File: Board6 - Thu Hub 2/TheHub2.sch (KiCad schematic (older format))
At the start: 26 parts, among them J1 12V Power, J2 SERVO, J3 I2C, U1 BNO055-Breakout, U2 FeatherM0, U3 RFM95-Breakout, U4 AZ1117-3.3, U5 L7806, U6 GT-U7_GPS

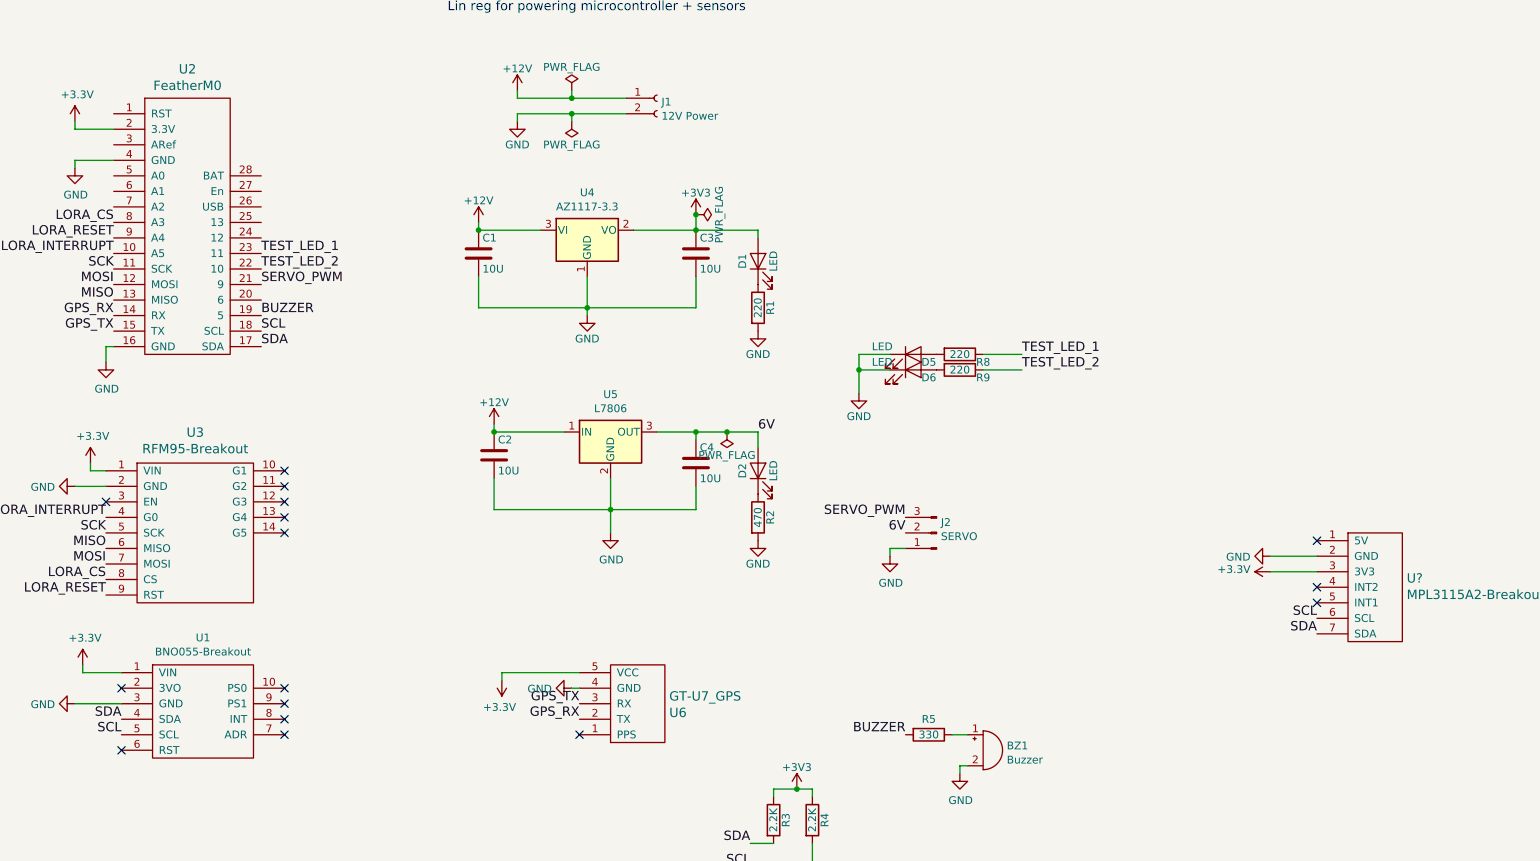
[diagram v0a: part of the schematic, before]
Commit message: For Hub2: add servo2 and GPS changed to breakout for MAX M8Q
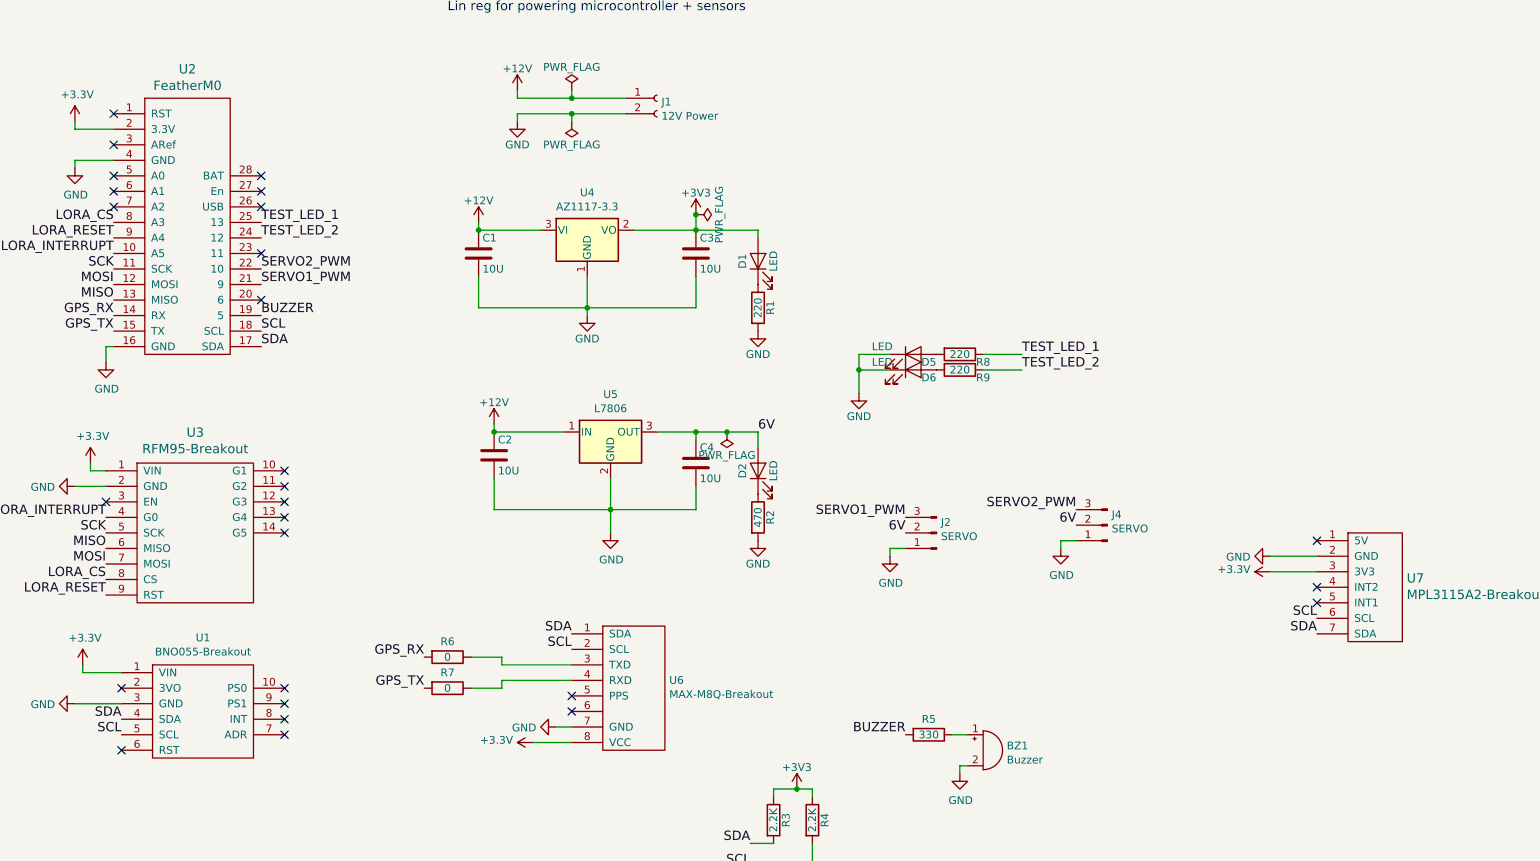
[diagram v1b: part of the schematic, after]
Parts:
- removed U6: GT-U7_GPS, DannysLib:GPS_GT-07, symbol Danny's_Lib:GT-U7_GPS
- added J4: SERVO, Pin_Headers:Pin_Header_Straight_1x03_Pitch2.54mm, symbol Connector:Conn_01x03_Male
- added R6, R7: 0, Resistors_SMD:R_0805, symbol Device:R
- added U6: MAX-M8Q-Breakout, DannysLib:MAX-M8Q-Breakout, symbol Danny's_Lib:MAX-M8Q-Breakout
- U7: renamed from U?; footprint (none) -> DannysLib:MPL3115A2-Breakout
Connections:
- net +3V3: now also U6.8 (VCC)
- net 6V: now also J4.2 (Pin_2)
- net GND: now also J4.1 (Pin_1), U6.7 (GND)
- net GPS_RX: now also R6.2
- net GPS_TX: now also R7.2
- net SCL: now also U6.2 (SCL)
- net SDA: now also U6.1 (SDA)
- net TEST_LED_1: now also U2.25 (13); no longer U2.23 (11)
- net TEST_LED_2: now also U2.24 (12); no longer U2.22 (10)
- net SERVO_PWM renamed SERVO1_PWM
- new net: R6.1, U6.3 (TXD)
- new net: R7.1, U6.4 (RXD)
- new net SERVO2_PWM: J4.3 (Pin_3), U2.22 (10)
- no-connect marks 16 -> 27
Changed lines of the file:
@@
 	9100 6650 8900 6650
 Text Label 10250 7200 2    60   ~ 0
-SERVO_PWM
+SERVO1_PWM
 Text Label 10250 7300 2    60   ~ 0
 6V
@@
 	10150 7400 10250 7400
 $Comp
-L Danny's_Lib:GT-U7_GPS U6
-U 1 1 5CB0ED28
-P 8550 8400
-F 0 "U6" H 8728 8458 60  0000 L CNN
-F 1 "GT-U7_GPS" H 8728 8352 60  0000 L CNN
-F 2 "DannysLib:GPS_GT-07" H 8700 8150 60  0001 C CNN
-F 3 "" H 8700 8150 60  0001 C CNN
-	1    8550 8400
-	1    0    0    1
-$EndComp
-NoConn ~ 8150 8600
-$Comp
 L Danny's_Lib:FeatherM0 U2
 U 1 1 5CB12923
@@
 Text Label 5150 6000 2    60   ~ 0
 GPS_TX
-Text Label 8150 8400 2    60   ~ 0
+Text Label 7150 8300 2    60   ~ 0
 GPS_TX
-Text Label 8150 8500 2    60   ~ 0
+Text Label 7150 8100 2    60   ~ 0
 GPS_RX
 Text Label 5150 5900 2    60   ~ 0
 GPS_RX
-$Comp
-L power:GND #PWR014
-U 1 1 5CB18900
-P 8100 8300
-F 0 "#PWR014" H 8100 8050 50  0001 C CNN
-F 1 "GND" V 8105 8172 50  0000 R CNN
-F 2 "" H 8100 8300 50  0001 C CNN
-F 3 "" H 8100 8300 50  0001 C CNN
-	1    8100 8300
-	0    1    1    0
-$EndComp
-Wire Wire Line
-	8100 8300 8150 8300
-$Comp
-L power:+3.3V #PWR013
-U 1 1 5CB1A329
-P 7650 8250
-F 0 "#PWR013" H 7650 8100 50  0001 C CNN
-F 1 "+3.3V" H 7665 8423 50  0000 C CNN
-F 2 "" H 7650 8250 50  0001 C CNN
-F 3 "" H 7650 8250 50  0001 C CNN
-	1    7650 8250
-	-1   0    0    1
-$EndComp
-Wire Wire Line
-	7650 8250 7650 8200
-Wire Wire Line
-	7650 8200 8150 8200
 $Comp
 L power:GND #PWR011
@@
 BUZZER
 Text Label 6100 5700 0    60   ~ 0
-SERVO_PWM
+SERVO1_PWM
 Text Label 11000 6150 0    60   ~ 0
 TEST_LED_1
-Text Label 6100 5600 0    60   ~ 0
+Text Label 6100 5400 0    60   ~ 0
 TEST_LED_2
-Text Label 6100 5500 0    60   ~ 0
+Text Label 6100 5300 0    60   ~ 0
 TEST_LED_1
 $Comp
@@
 	4900 4900 5150 4900
 $Comp
-L Danny's_Lib:MPL3115A2-Breakout U?
+L Danny's_Lib:MPL3115A2-Breakout U7
 U 1 1 5CC5A3F2
 P 13250 7650
-F 0 "U?" H 13478 7708 60  0000 L CNN
+F 0 "U7" H 13478 7708 60  0000 L CNN
 F 1 "MPL3115A2-Breakout" H 13478 7602 60  0000 L CNN
-F 2 "" V 13100 7500 60  0001 C CNN
+F 2 "DannysLib:MPL3115A2-Breakout" V 13100 7500 60  0001 C CNN
 F 3 "" V 13100 7500 60  0001 C CNN
 	1    13250 7650
@@
 $EndComp
 $Comp
-L power:+3.3V #PWR?
+L power:+3.3V #PWR0103
 U 1 1 5CC5AE7C
 P 12600 7550
-F 0 "#PWR?" H 12600 7400 50  0001 C CNN
+F 0 "#PWR0103" H 12600 7400 50  0001 C CNN
 F 1 "+3.3V" V 12615 7678 50  0000 L CNN
 F 2 "" H 12600 7550 50  0001 C CNN
@@
 	12600 7550 12900 7550
 $Comp
-L power:GND #PWR?
+L power:GND #PWR0104
 U 1 1 5CC5D6E7
 P 12600 7450
-F 0 "#PWR?" H 12600 7200 50  0001 C CNN
+F 0 "#PWR0104" H 12600 7200 50  0001 C CNN
 F 1 "GND" V 12605 7322 50  0000 R CNN
 F 2 "" H 12600 7450 50  0001 C CNN
@@
 NoConn ~ 12900 7650
 NoConn ~ 12900 7350
+Text Label 11350 7150 2    60   ~ 0
+SERVO2_PWM
+Text Label 11350 7250 2    60   ~ 0
+6V
+$Comp
+L power:GND #PWR0105
+U 1 1 5CAC3301
+P 11250 7400
+F 0 "#PWR0105" H 11250 7150 50  0001 C CNN
+F 1 "GND" H 11255 7227 50  0000 C CNN
+F 2 "" H 11250 7400 50  0001 C CNN
+F 3 "" H 11250 7400 50  0001 C CNN
+	1    11250 7400
+	1    0    0    -1
+$EndComp
+Wire Wire Line
+	11250 7400 11250 7350
+Wire Wire Line
+	11250 7350 11350 7350
+$Comp
+L Connector:Conn_01x03_Male J4
+U 1 1 5CAC3309
+P 11550 7250
+F 0 "J4" H 11522 7182 50  0000 R CNN
+F 1 "SERVO" H 11522 7273 50  0000 R CNN
+F 2 "Pin_Headers:Pin_Header_Straight_1x03_Pitch2.54mm" H 11550 7250 50  0001 C CNN
+F 3 "~" H 11550 7250 50  0001 C CNN
+	1    11550 7250
+	-1   0    0    1
+$EndComp
+Text Label 6100 5600 0    60   ~ 0
+SERVO2_PWM
+$Comp
+L Danny's_Lib:MAX-M8Q-Breakout U6
+U 1 1 5CAC4EC0
+P 8500 8300
+F 0 "U6" H 8728 8351 50  0000 L CNN
+F 1 "MAX-M8Q-Breakout" H 8728 8260 50  0000 L CNN
+F 2 "DannysLib:MAX-M8Q-Breakout" H 8550 8350 50  0001 C CNN
+F 3 "" H 8550 8350 50  0001 C CNN
+	1    8500 8300
+	1    0    0    -1
+$EndComp
+Text Label 8100 7950 2    60   ~ 0
+SDA
+Text Label 8100 8050 2    60   ~ 0
+SCL
+NoConn ~ 8100 8350
+NoConn ~ 8100 8450
+$Comp
+L power:GND #PWR0106
+U 1 1 5CAC9F48
+P 8000 8550
+F 0 "#PWR0106" H 8000 8300 50  0001 C CNN
+F 1 "GND" V 8005 8422 50  0000 R CNN
+F 2 "" H 8000 8550 50  0001 C CNN
+F 3 "" H 8000 8550 50  0001 C CNN
+	1    8000 8550
+	0    1    1    0
+$EndComp
+Wire Wire Line
+	8000 8550 8100 8550
+$Comp
+L power:+3.3V #PWR0107
+U 1 1 5CACBF38
+P 7850 8650
+F 0 "#PWR0107" H 7850 8500 50  0001 C CNN
+F 1 "+3.3V" V 7865 8778 50  0000 L CNN
+F 2 "" H 7850 8650 50  0001 C CNN
+F 3 "" H 7850 8650 50  0001 C CNN
+	1    7850 8650
+	0    -1   -1   0
+$EndComp
+Wire Wire Line
+	7850 8650 8100 8650
+$Comp
+L Device:R R6
+U 1 1 5CAD4F0B
+P 7300 8100
+F 0 "R6" V 7200 8100 50  0000 C CNN
+F 1 "0" V 7300 8100 50  0000 C CNN
+F 2 "Resistors_SMD:R_0805" V 7230 8100 50  0001 C CNN
+F 3 "~" H 7300 8100 50  0001 C CNN
+	1    7300 8100
+	0    1    1    0
+$EndComp
+$Comp
+L Device:R R7
+U 1 1 5CAD7B5D
+P 7300 8300
+F 0 "R7" V 7200 8300 50  0000 C CNN
+F 1 "0" V 7300 8300 50  0000 C CNN
+F 2 "Resistors_SMD:R_0805" V 7230 8300 50  0001 C CNN
+F 3 "~" H 7300 8300 50  0001 C CNN
+	1    7300 8300
+	0    1    1    0
+$EndComp
+Wire Wire Line
+	7450 8300 7650 8300
+Wire Wire Line
+	7650 8300 7650 8250
+Wire Wire Line
+	7650 8250 8100 8250
+Wire Wire Line
+	7450 8100 7650 8100
+Wire Wire Line
+	7650 8100 7650 8150
+Wire Wire Line
+	7650 8150 8100 8150
+NoConn ~ 6100 5000
+NoConn ~ 6100 5100
+NoConn ~ 6100 5200
+NoConn ~ 6100 5500
+NoConn ~ 6100 5800
+NoConn ~ 5150 5200
+NoConn ~ 5150 5100
+NoConn ~ 5150 5000
+NoConn ~ 5150 4800
+NoConn ~ 5150 4600
 $EndSCHEMATC
